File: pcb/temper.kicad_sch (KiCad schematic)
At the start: 0 parts

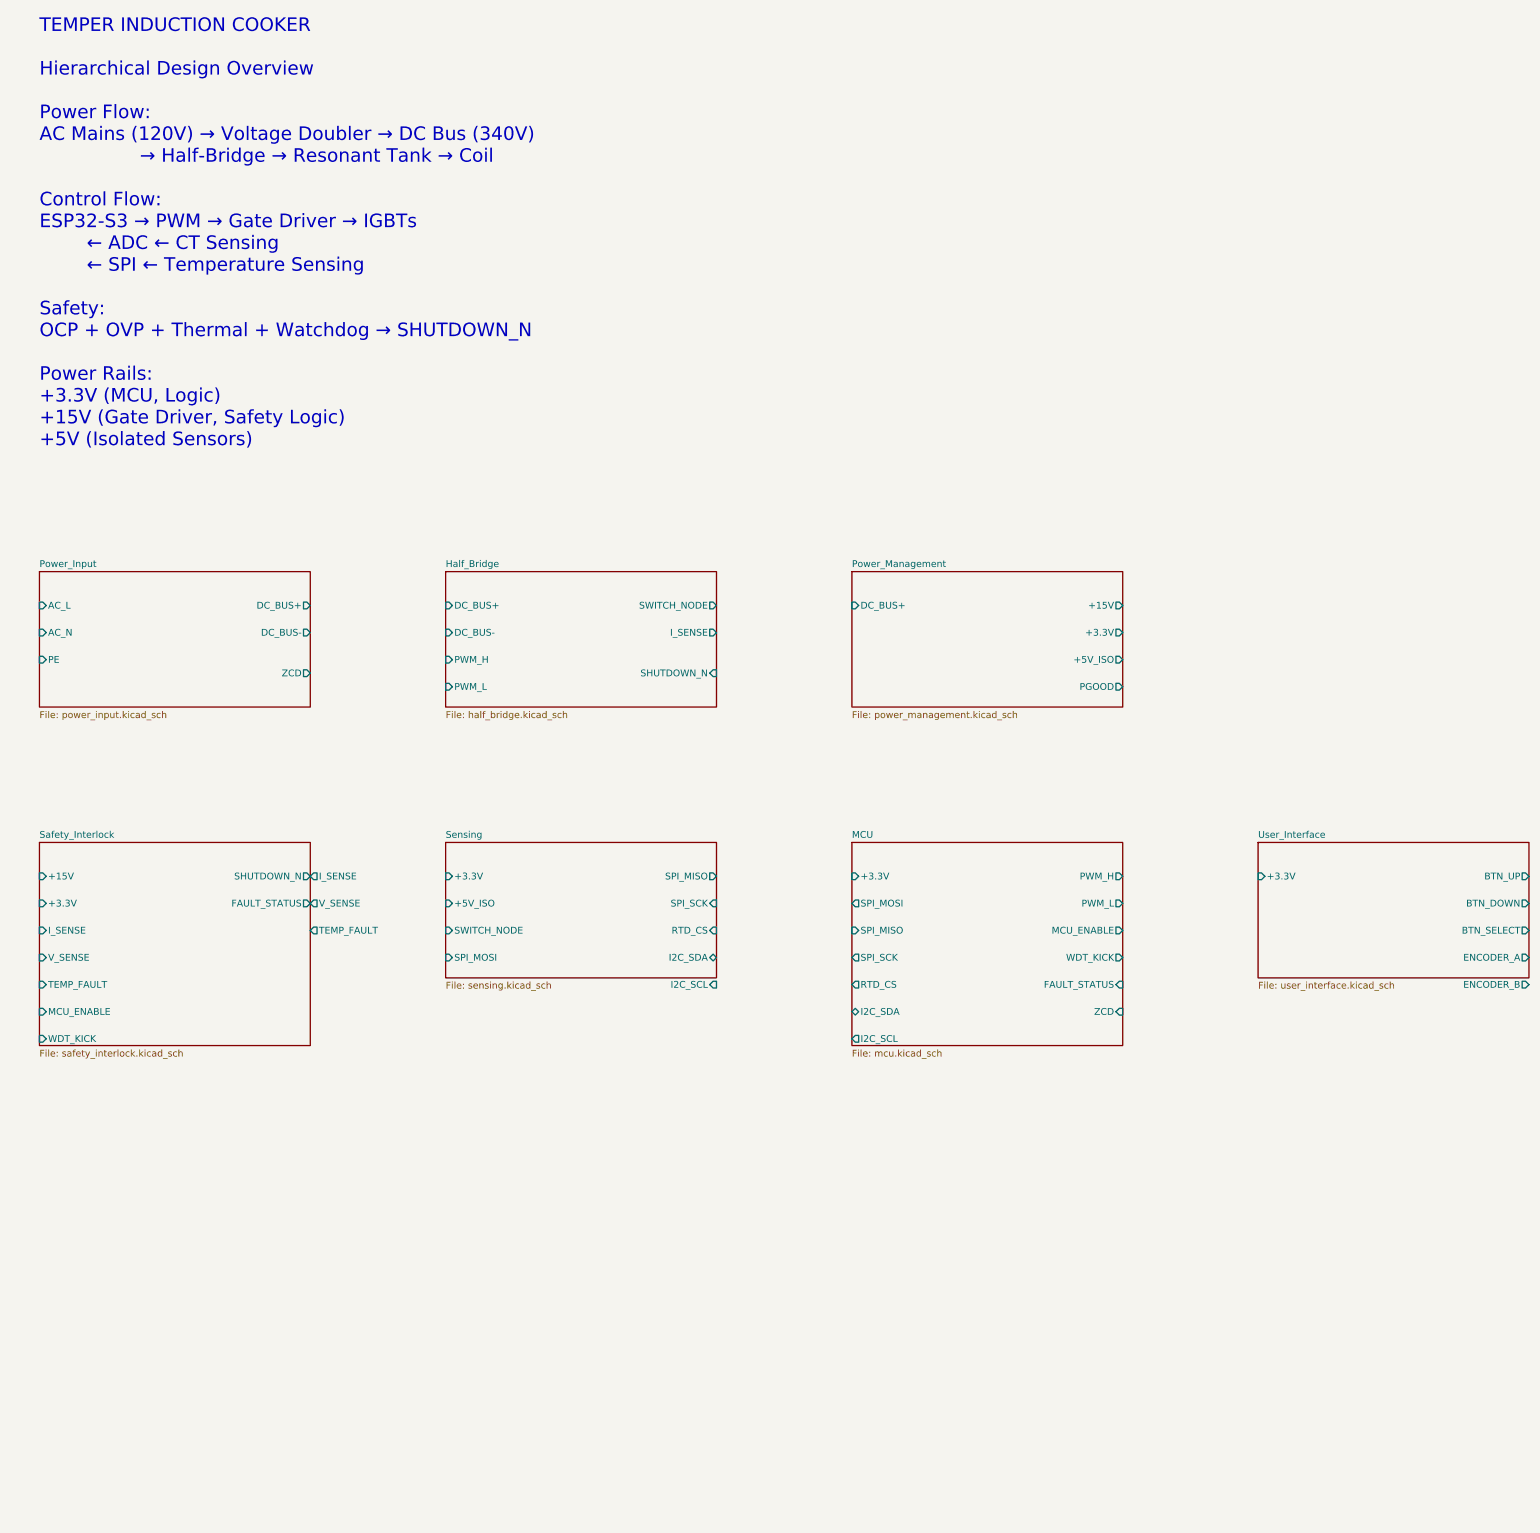
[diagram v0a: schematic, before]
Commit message: fix: wire root-level cross-sheet nets in temper.kicad_sch
The top-level hierarchical sheet had zero wires and zero labels -
seven sheet-symbol blocks with pins but nothing connecting them, so
none of the per-sheet fixes in the previous commit could actually
reach each other end-to-end.

Wired 16 confirmed-clean nets: DC_BUS+ (4-way), DC_BUS-, PWM_H, PWM_L,
SHUTDOWN_N, ZCD, WDT_KICK, FAULT_STATUS, SPI_MOSI/MISO/SCK, RTD_CS,
I2C_SDA/SCL, RELAY_CTRL, RTD_DRDY. Added 5 missing root sheet-pins
along the way (Safety_Interlock DC_BUS+, Power_Input RELAY_CTRL, MCU
RELAY_CTRL+RTD_DRDY, Sensing RTD_DRDY).

Caught a real bug while verifying: Sensing's I_SENSE/V_SENSE/TEMP_FAULT
root pins were sitting at Safety_Interlock's coordinates (a copy-paste
layout error), which would have silently shorted SHUTDOWN_N and
FAULT_STATUS to unrelated Sensing signals the instant they were wired.
Caught by the same connectivity tracer used throughout, before the fix
was considered done, and relocated to Sensing's own sheet box.

Deliberately left unwired: I_SENSE (unresolved duplicate-producer
conflict between Half_Bridge and Sensing), +5V_ISO/GND_ISO (missing
regulator), MCU_ENABLE routing into Safety_Interlock, and
User_Interface's fault-LED signals (its root pins are still stale
placeholders for a button/encoder UI that was never implemented).

Co-Authored-By: Claude Sonnet 5 <noreply@anthropic.com>
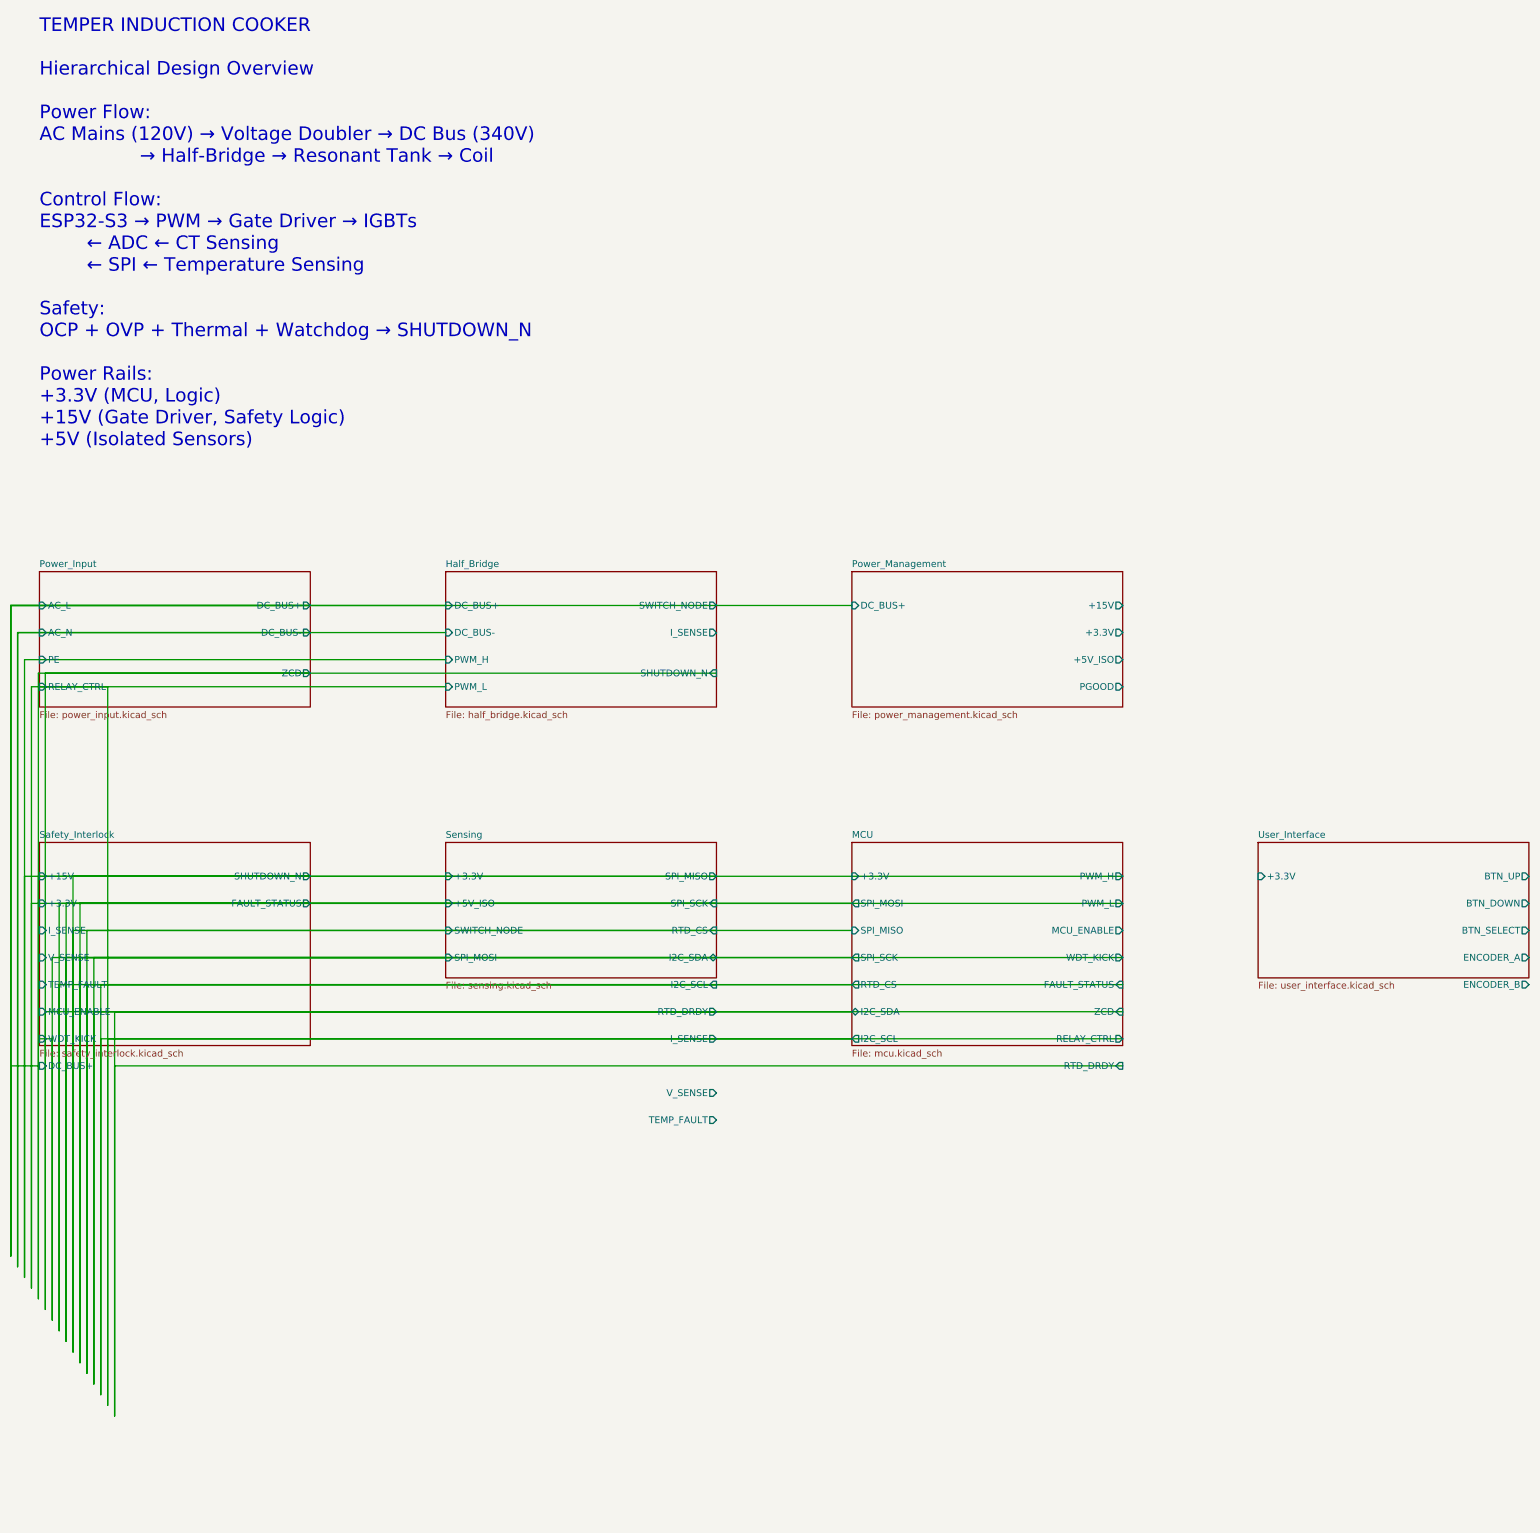
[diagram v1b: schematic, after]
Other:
- sheet MCU ports: added RELAY_CTRL, RTD_DRDY; removed none
- sheet Power_Input ports: added RELAY_CTRL; removed none
- sheet Safety_Interlock ports: added DC_BUS+; removed none
- sheet Sensing ports: added RTD_DRDY; removed none
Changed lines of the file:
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@@
+      )
+    )
+    (pin "RELAY_CTRL" input
+      (at 25.4 123.19 180)
+      (effects
+        (font
+          (size 1.27 1.27)
+        )
+        (justify left)
       )
     )
@@
       )
     )
+    (pin "DC_BUS+" input
+      (at 25.4 194.31 180)
+      (effects
+        (font
+          (size 1.27 1.27)
+        )
+        (justify left)
+      )
+    )
     (instances
       (project "temper"
@@
       )
     )
+    (pin "RTD_DRDY" output
+      (at 152.4 184.15 0)
+      (effects
+        (font
+          (size 1.27 1.27)
+        )
+        (justify right)
+      )
+    )
     (pin "I_SENSE" output
-      (at 76.2 158.75 180)
-      (effects
-        (font
-          (size 1.27 1.27)
-        )
-        (justify left)
+      (at 152.4 189.23 0)
+      (effects
+        (font
+          (size 1.27 1.27)
+        )
+        (justify right)
       )
     )
     (pin "V_SENSE" output
-      (at 76.2 163.83 180)
-      (effects
-        (font
-          (size 1.27 1.27)
-        )
-        (justify left)
+      (at 152.4 199.39 0)
+      (effects
+        (font
+          (size 1.27 1.27)
+        )
+        (justify right)
       )
     )
     (pin "TEMP_FAULT" output
-      (at 76.2 168.91 180)
-      (effects
-        (font
-          (size 1.27 1.27)
-        )
-        (justify left)
+      (at 152.4 204.47 0)
+      (effects
+        (font
+          (size 1.27 1.27)
+        )
+        (justify right)
       )
     )
@@
       )
     )
+    (pin "RELAY_CTRL" output
+      (at 228.6 189.23 0)
+      (effects
+        (font
+          (size 1.27 1.27)
+        )
+        (justify right)
+      )
+    )
+    (pin "RTD_DRDY" input
+      (at 228.6 194.31 0)
+      (effects
+        (font
+          (size 1.27 1.27)
+        )
+        (justify right)
+      )
+    )
     (instances
       (project "temper"
@@
     )
   )
+  (wire (pts (xy 76.2 107.95) (xy 20.0 107.95)) (stroke (width 0) (type default)))
+  (wire (pts (xy 20.0 107.95) (xy 20.0 230.0)) (stroke (width 0) (type default)))
+  (wire (pts (xy 101.6 107.95) (xy 20.0 107.95)) (stroke (width 0) (type default)))
+  (wire (pts (xy 20.0 107.95) (xy 20.0 230.0)) (stroke (width 0) (type default)))
+  (wire (pts (xy 177.8 107.95) (xy 20.0 107.95)) (stroke (width 0) (type default)))
+  (wire (pts (xy 20.0 107.95) (xy 20.0 230.0)) (stroke (width 0) (type default)))
+  (wire (pts (xy 25.4 194.31) (xy 20.0 194.31)) (stroke (width 0) (type default)))
+  (wire (pts (xy 20.0 194.31) (xy 20.0 230.0)) (stroke (width 0) (type default)))
+  (wire (pts (xy 76.2 113.03) (xy 21.3 113.03)) (stroke (width 0) (type default)))
+  (wire (pts (xy 21.3 113.03) (xy 21.3 232.0)) (stroke (width 0) (type default)))
+  (wire (pts (xy 101.6 113.03) (xy 21.3 113.03)) (stroke (width 0) (type default)))
+  (wire (pts (xy 21.3 113.03) (xy 21.3 232.0)) (stroke (width 0) (type default)))
+  (wire (pts (xy 101.6 118.11) (xy 22.6 118.11)) (stroke (width 0) (type default)))
+  (wire (pts (xy 22.6 118.11) (xy 22.6 234.0)) (stroke (width 0) (type default)))
+  (wire (pts (xy 228.6 158.75) (xy 22.6 158.75)) (stroke (width 0) (type default)))
+  (wire (pts (xy 22.6 158.75) (xy 22.6 234.0)) (stroke (width 0) (type default)))
+  (wire (pts (xy 101.6 123.19) (xy 23.9 123.19)) (stroke (width 0) (type default)))
+  (wire (pts (xy 23.9 123.19) (xy 23.9 236.0)) (stroke (width 0) (type default)))
+  (wire (pts (xy 228.6 163.83) (xy 23.9 163.83)) (stroke (width 0) (type default)))
+  (wire (pts (xy 23.9 163.83) (xy 23.9 236.0)) (stroke (width 0) (type default)))
+  (wire (pts (xy 152.4 120.65) (xy 25.2 120.65)) (stroke (width 0) (type default)))
+  (wire (pts (xy 25.2 120.65) (xy 25.2 238.0)) (stroke (width 0) (type default)))
+  (wire (pts (xy 76.2 158.75) (xy 25.2 158.75)) (stroke (width 0) (type default)))
+  (wire (pts (xy 25.2 158.75) (xy 25.2 238.0)) (stroke (width 0) (type default)))
+  (wire (pts (xy 76.2 120.65) (xy 26.5 120.65)) (stroke (width 0) (type default)))
+  (wire (pts (xy 26.5 120.65) (xy 26.5 240.0)) (stroke (width 0) (type default)))
+  (wire (pts (xy 228.6 184.15) (xy 26.5 184.15)) (stroke (width 0) (type default)))
+  (wire (pts (xy 26.5 184.15) (xy 26.5 240.0)) (stroke (width 0) (type default)))
+  (wire (pts (xy 25.4 189.23) (xy 27.8 189.23)) (stroke (width 0) (type default)))
+  (wire (pts (xy 27.8 189.23) (xy 27.8 242.0)) (stroke (width 0) (type default)))
+  (wire (pts (xy 228.6 173.99) (xy 27.8 173.99)) (stroke (width 0) (type default)))
+  (wire (pts (xy 27.8 173.99) (xy 27.8 242.0)) (stroke (width 0) (type default)))
+  (wire (pts (xy 76.2 163.83) (xy 29.1 163.83)) (stroke (width 0) (type default)))
+  (wire (pts (xy 29.1 163.83) (xy 29.1 244.0)) (stroke (width 0) (type default)))
+  (wire (pts (xy 228.6 179.07) (xy 29.1 179.07)) (stroke (width 0) (type default)))
+  (wire (pts (xy 29.1 179.07) (xy 29.1 244.0)) (stroke (width 0) (type default)))
+  (wire (pts (xy 101.6 173.99) (xy 30.4 173.99)) (stroke (width 0) (type default)))
+  (wire (pts (xy 30.4 173.99) (xy 30.4 246.0)) (stroke (width 0) (type default)))
+  (wire (pts (xy 177.8 163.83) (xy 30.4 163.83)) (stroke (width 0) (type default)))
+  (wire (pts (xy 30.4 163.83) (xy 30.4 246.0)) (stroke (width 0) (type default)))
+  (wire (pts (xy 152.4 158.75) (xy 31.7 158.75)) (stroke (width 0) (type default)))
+  (wire (pts (xy 31.7 158.75) (xy 31.7 248.0)) (stroke (width 0) (type default)))
+  (wire (pts (xy 177.8 168.91) (xy 31.7 168.91)) (stroke (width 0) (type default)))
+  (wire (pts (xy 31.7 168.91) (xy 31.7 248.0)) (stroke (width 0) (type default)))
+  (wire (pts (xy 152.4 163.83) (xy 33.0 163.83)) (stroke (width 0) (type default)))
+  (wire (pts (xy 33.0 163.83) (xy 33.0 250.0)) (stroke (width 0) (type default)))
+  (wire (pts (xy 177.8 173.99) (xy 33.0 173.99)) (stroke (width 0) (type default)))
+  (wire (pts (xy 33.0 173.99) (xy 33.0 250.0)) (stroke (width 0) (type default)))
+  (wire (pts (xy 152.4 168.91) (xy 34.3 168.91)) (stroke (width 0) (type default)))
+  (wire (pts (xy 34.3 168.91) (xy 34.3 252.0)) (stroke (width 0) (type default)))
+  (wire (pts (xy 177.8 179.07) (xy 34.3 179.07)) (stroke (width 0) (type default)))
+  (wire (pts (xy 34.3 179.07) (xy 34.3 252.0)) (stroke (width 0) (type default)))
+  (wire (pts (xy 152.4 173.99) (xy 35.6 173.99)) (stroke (width 0) (type default)))
+  (wire (pts (xy 35.6 173.99) (xy 35.6 254.0)) (stroke (width 0) (type default)))
+  (wire (pts (xy 177.8 184.15) (xy 35.6 184.15)) (stroke (width 0) (type default)))
+  (wire (pts (xy 35.6 184.15) (xy 35.6 254.0)) (stroke (width 0) (type default)))
+  (wire (pts (xy 152.4 179.07) (xy 36.9 179.07)) (stroke (width 0) (type default)))
+  (wire (pts (xy 36.9 179.07) (xy 36.9 256.0)) (stroke (width 0) (type default)))
+  (wire (pts (xy 177.8 189.23) (xy 36.9 189.23)) (stroke (width 0) (type default)))
+  (wire (pts (xy 36.9 189.23) (xy 36.9 256.0)) (stroke (width 0) (type default)))
+  (wire (pts (xy 25.4 123.19) (xy 38.2 123.19)) (stroke (width 0) (type default)))
+  (wire (pts (xy 38.2 123.19) (xy 38.2 258.0)) (stroke (width 0) (type default)))
+  (wire (pts (xy 228.6 189.23) (xy 38.2 189.23)) (stroke (width 0) (type default)))
+  (wire (pts (xy 38.2 189.23) (xy 38.2 258.0)) (stroke (width 0) (type default)))
+  (wire (pts (xy 152.4 184.15) (xy 39.5 184.15)) (stroke (width 0) (type default)))
+  (wire (pts (xy 39.5 184.15) (xy 39.5 260.0)) (stroke (width 0) (type default)))
+  (wire (pts (xy 228.6 194.31) (xy 39.5 194.31)) (stroke (width 0) (type default)))
+  (wire (pts (xy 39.5 194.31) (xy 39.5 260.0)) (stroke (width 0) (type default)))
 )
